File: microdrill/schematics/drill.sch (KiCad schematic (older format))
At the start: 7 parts, among them P7 CONN_2

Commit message: Testet automatic drill speed management
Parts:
- added C6: 47u, symbol CP1
- R4: value 1k -> 47k
- gave numbers to parts that had none: 2
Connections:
- net GND: now also C6.2
- net Sence: now also C6.1
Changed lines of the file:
@@
 Sheet 2 2
 Title ""
-Date "17 aug 2014"
+Date "19 aug 2014"
 Rev ""
 Comp ""
@@
 Motor
 $Comp
-L GND #PWR028
+L GND #PWR030
 U 1 1 53E67E30
 P 4800 5700
-F 0 "#PWR028" H 4800 5700 30  0001 C CNN
+F 0 "#PWR030" H 4800 5700 30  0001 C CNN
 F 1 "GND" H 4800 5630 30  0001 C CNN
 F 2 "" H 4800 5700 60  0000 C CNN
@@
 $EndComp
 $Comp
-L +12V #PWR029
+L +12V #PWR031
 U 1 1 53E67FAE
 P 5375 3200
-F 0 "#PWR029" H 5375 3150 20  0001 C CNN
+F 0 "#PWR031" H 5375 3150 20  0001 C CNN
 F 1 "+12V" H 5375 3300 30  0000 C CNN
 F 2 "" H 5375 3200 60  0000 C CNN
@@
 P 4350 5100
 F 0 "R4" V 4430 5100 50  0000 C CNN
-F 1 "1k" V 4350 5100 50  0000 C CNN
+F 1 "47k" V 4350 5100 50  0000 C CNN
 F 2 "" H 4350 5100 60  0000 C CNN
 F 3 "" H 4350 5100 60  0000 C CNN
@@
 	4550 4350 3200 4350
 $Comp
-L S8205A VT?
+L S8205A VT1
 U 1 1 53F123C0
 P 5300 4150
-F 0 "VT?" H 5375 3775 60  0000 R CNN
+F 0 "VT1" H 5375 3775 60  0000 R CNN
 F 1 "S8205A" H 5450 4500 60  0000 R CNN
 F 2 "TSSOP-8" H 5250 3850 60  0001 C CNN
@@
 	6050 4600 6050 4350
 $Comp
-L R R?
+L R R7
 U 1 1 53F123DF
 P 5100 5350
-F 0 "R?" V 5180 5350 50  0000 C CNN
+F 0 "R7" V 5180 5350 50  0000 C CNN
 F 1 "1R" V 5100 5350 50  0000 C CNN
 F 2 "" H 5100 5350 60  0000 C CNN
@@
 	6050 3700 6050 3950
 Connection ~ 5375 3700
+$Comp
+L GND #PWR032
+U 1 1 53F35910
+P 4000 5700
+F 0 "#PWR032" H 4000 5700 30  0001 C CNN
+F 1 "GND" H 4000 5630 30  0001 C CNN
+F 2 "" H 4000 5700 60  0000 C CNN
+F 3 "" H 4000 5700 60  0000 C CNN
+	1    4000 5700
+	1    0    0    -1
+$EndComp
+Wire Wire Line
+	4000 5700 4000 5600
+Wire Wire Line
+	4000 5200 4000 5100
+Connection ~ 4000 5100
+$Comp
+L CP1 C6
+U 1 1 53F36070
+P 4000 5400
+F 0 "C6" H 4050 5500 50  0000 L CNN
+F 1 "47u" H 4050 5300 50  0000 L CNN
+F 2 "" H 4000 5400 60  0000 C CNN
+F 3 "" H 4000 5400 60  0000 C CNN
+	1    4000 5400
+	1    0    0    -1
+$EndComp
 $EndSCHEMATC

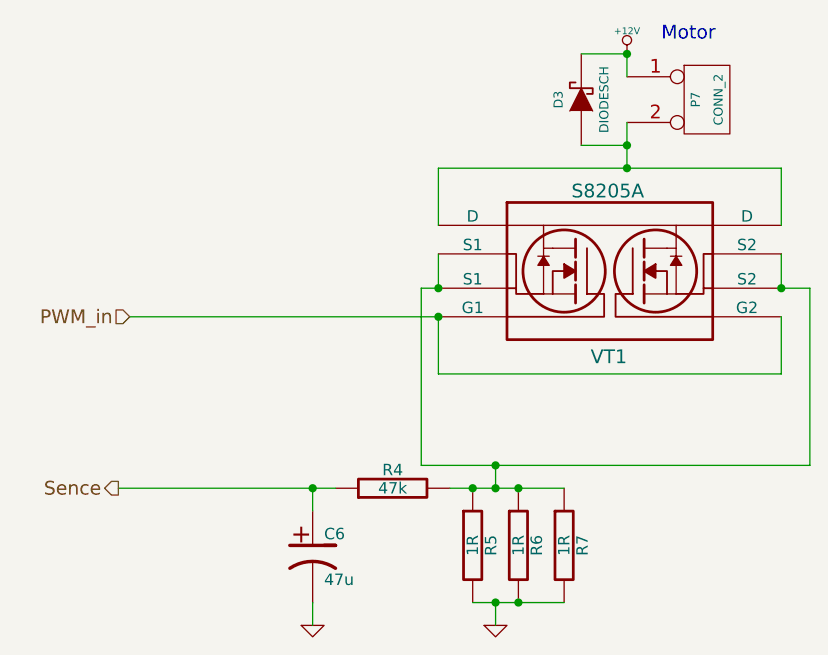
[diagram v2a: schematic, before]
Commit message: started voltmeter hacking
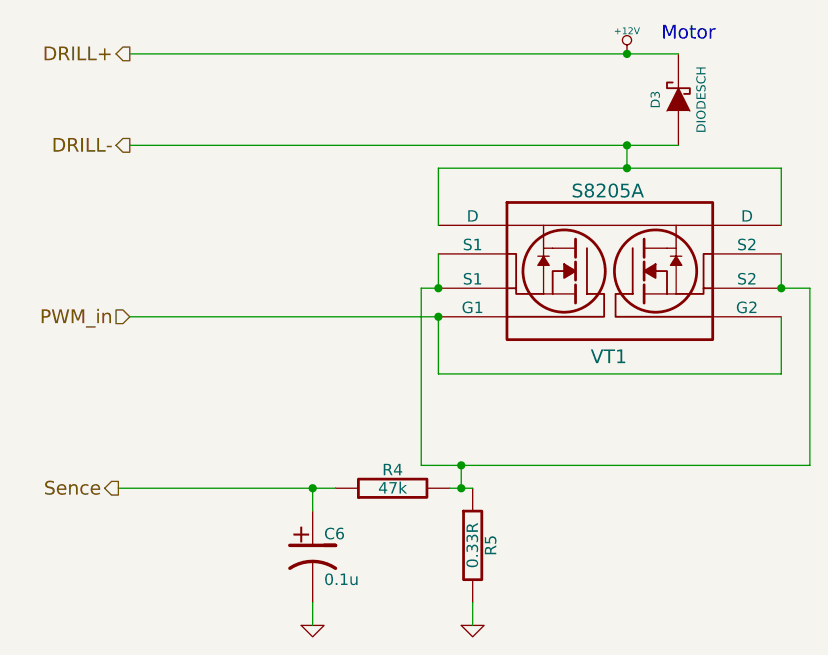
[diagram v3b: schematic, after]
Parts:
- removed P7: CONN_2, symbol CONN_2
- removed R6, R7: 1R, symbol R
- C6: value 47u -> 0.1u; footprint (none) -> SM0603
- R5: value 1R -> 0.33R; footprint (none) -> SM2512
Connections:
- net DRILL-: now reaches D3.1 (A), VT1.1 (D), VT1.8 (D)
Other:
- moved on the sheet: D3
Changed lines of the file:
@@
 LIBS:s8205a
 LIBS:MCU_module-cache
-EELAYER 27 0
+EELAYER 24 0
 EELAYER END
 $Descr A4 11693 8268
@@
 Sheet 2 2
 Title ""
-Date "20 oct 2014"
+Date "14 nov 2014"
 Rev ""
 Comp ""
@@
 Comment4 ""
 $EndDescr
-$Comp
-L CONN_2 P7
-U 1 1 53E67E05
-P 5725 3400
-F 0 "P7" V 5675 3400 40  0000 C CNN
-F 1 "CONN_2" V 5775 3400 40  0000 C CNN
-F 2 "" H 5725 3400 60  0000 C CNN
-F 3 "" H 5725 3400 60  0000 C CNN
-	1    5725 3400
-	1    0    0    -1
-$EndComp
 Text Notes 5525 3150 0    60   ~ 0
 Motor
 $Comp
-L GND #PWR28
+L GND #PWR016
 U 1 1 53E67E30
-P 4800 5700
-F 0 "#PWR28" H 4800 5700 30  0001 C CNN
-F 1 "GND" H 4800 5630 30  0001 C CNN
-F 2 "" H 4800 5700 60  0000 C CNN
-F 3 "" H 4800 5700 60  0000 C CNN
-	1    4800 5700
+P 4700 5700
+F 0 "#PWR016" H 4700 5700 30  0001 C CNN
+F 1 "GND" H 4700 5630 30  0001 C CNN
+F 2 "" H 4700 5700 60  0000 C CNN
+F 3 "" H 4700 5700 60  0000 C CNN
+	1    4700 5700
 	1    0    0    -1
 $EndComp
@@
 P 4700 5350
 F 0 "R5" V 4780 5350 50  0000 C CNN
-F 1 "1R" V 4700 5350 50  0000 C CNN
-F 2 "" H 4700 5350 60  0000 C CNN
+F 1 "0.33R" V 4700 5350 50  0000 C CNN
+F 2 "SM2512" H 4700 5350 60  0001 C CNN
 F 3 "" H 4700 5350 60  0000 C CNN
 	1    4700 5350
@@
 $EndComp
 $Comp
-L R R6
-U 1 1 53E67E9C
-P 4900 5350
-F 0 "R6" V 4980 5350 50  0000 C CNN
-F 1 "1R" V 4900 5350 50  0000 C CNN
-F 2 "" H 4900 5350 60  0000 C CNN
-F 3 "" H 4900 5350 60  0000 C CNN
-	1    4900 5350
-	1    0    0    -1
-$EndComp
-$Comp
-L +12V #PWR29
+L +12V #PWR017
 U 1 1 53E67FAE
 P 5375 3200
-F 0 "#PWR29" H 5375 3150 20  0001 C CNN
+F 0 "#PWR017" H 5375 3150 20  0001 C CNN
 F 1 "+12V" H 5375 3300 30  0000 C CNN
 F 2 "" H 5375 3200 60  0000 C CNN
@@
 	0    -1   -1   0
 $EndComp
-Wire Wire Line
-	4800 5700 4800 5600
-Wire Wire Line
-	5375 3200 5375 3300
-Wire Wire Line
-	4600 5100 5100 5100
-Wire Wire Line
-	4800 5000 4800 5100
-Connection ~ 4800 5100
-Wire Wire Line
-	4700 5600 5100 5600
-Connection ~ 4800 5600
-Connection ~ 4700 5100
-Wire Wire Line
-	5375 3500 5375 3700
 $Comp
 L DIODESCH D3
 U 1 1 53E68EA1
-P 5175 3400
-F 0 "D3" H 5175 3500 40  0000 C CNN
-F 1 "DIODESCH" H 5175 3300 40  0000 C CNN
-F 2 "" H 5175 3400 60  0000 C CNN
-F 3 "" H 5175 3400 60  0000 C CNN
-	1    5175 3400
+P 5600 3400
+F 0 "D3" H 5600 3500 40  0000 C CNN
+F 1 "DIODESCH" H 5600 3300 40  0000 C CNN
+F 2 "" H 5600 3400 60  0000 C CNN
+F 3 "" H 5600 3400 60  0000 C CNN
+	1    5600 3400
 	0    -1   -1   0
 $EndComp
-Wire Wire Line
-	5175 3200 5375 3200
-Connection ~ 5375 3200
-Wire Wire Line
-	5175 3600 5375 3600
-Connection ~ 5375 3600
 Text HLabel 3200 4350 0    60   Input ~ 0
 PWM_in
 Text HLabel 3150 5100 0    60   Output ~ 0
 Sence
-Wire Wire Line
-	3150 5100 4100 5100
-Wire Wire Line
-	4550 4350 3200 4350
 $Comp
 L S8205A VT1
@@
 	1    0    0    -1
 $EndComp
+$Comp
+L GND #PWR018
+U 1 1 53F35910
+P 4000 5700
+F 0 "#PWR018" H 4000 5700 30  0001 C CNN
+F 1 "GND" H 4000 5630 30  0001 C CNN
+F 2 "" H 4000 5700 60  0000 C CNN
+F 3 "" H 4000 5700 60  0000 C CNN
+	1    4000 5700
+	1    0    0    -1
+$EndComp
+$Comp
+L CP1 C6
+U 1 1 53F36070
+P 4000 5400
+F 0 "C6" H 4050 5500 50  0000 L CNN
+F 1 "0.1u" H 4050 5300 50  0000 L CNN
+F 2 "SM0603" H 4000 5400 60  0001 C CNN
+F 3 "" H 4000 5400 60  0000 C CNN
+	1    4000 5400
+	1    0    0    -1
+$EndComp
+Wire Wire Line
+	3200 3200 5600 3200
+Connection ~ 5375 3200
+Wire Wire Line
+	3200 3600 5600 3600
+Connection ~ 5375 3600
+Wire Wire Line
+	3150 5100 4100 5100
+Wire Wire Line
+	4550 4350 3200 4350
 Connection ~ 4550 4350
 Wire Wire Line
@@
 Wire Wire Line
 	6050 4600 6050 4350
-$Comp
-L R R7
-U 1 1 53F123DF
-P 5100 5350
-F 0 "R7" V 5180 5350 50  0000 C CNN
-F 1 "1R" V 5100 5350 50  0000 C CNN
-F 2 "" H 5100 5350 60  0000 C CNN
-F 3 "" H 5100 5350 60  0000 C CNN
-	1    5100 5350
-	1    0    0    -1
-$EndComp
-Connection ~ 4900 5600
-Connection ~ 4900 5100
 Wire Wire Line
 	4550 4075 4550 4225
@@
 Wire Wire Line
 	6175 4225 6050 4225
-Connection ~ 4800 5000
 Connection ~ 6050 4225
 Connection ~ 4550 4225
@@
 	6050 3700 6050 3950
 Connection ~ 5375 3700
-$Comp
-L GND #PWR27
-U 1 1 53F35910
-P 4000 5700
-F 0 "#PWR27" H 4000 5700 30  0001 C CNN
-F 1 "GND" H 4000 5630 30  0001 C CNN
-F 2 "" H 4000 5700 60  0000 C CNN
-F 3 "" H 4000 5700 60  0000 C CNN
-	1    4000 5700
-	1    0    0    -1
-$EndComp
 Wire Wire Line
 	4000 5700 4000 5600
@@
 	4000 5200 4000 5100
 Connection ~ 4000 5100
-$Comp
-L CP1 C6
-U 1 1 53F36070
-P 4000 5400
-F 0 "C6" H 4050 5500 50  0000 L CNN
-F 1 "47u" H 4050 5300 50  0000 L CNN
-F 2 "" H 4000 5400 60  0000 C CNN
-F 3 "" H 4000 5400 60  0000 C CNN
-	1    4000 5400
-	1    0    0    -1
-$EndComp
+Wire Wire Line
+	4700 5700 4700 5600
+Wire Wire Line
+	4700 5100 4600 5100
+Wire Wire Line
+	4650 5100 4650 5000
+Connection ~ 4650 5000
+Connection ~ 4650 5100
+Wire Wire Line
+	5375 3700 5375 3600
+Text HLabel 3200 3200 0    60   Output ~ 0
+DRILL+
+Text HLabel 3200 3600 0    60   Output ~ 0
+DRILL-
 $EndSCHEMATC
